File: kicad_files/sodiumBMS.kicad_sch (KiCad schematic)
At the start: 28 parts, among them J1 USB_C_Receptacle_PowerOnly_6P, Q1 AO3400A, U1 STM32F446RETx, U2 INA180A4, U3 INA180A4, U4 LM3940, U5 MC34063AD

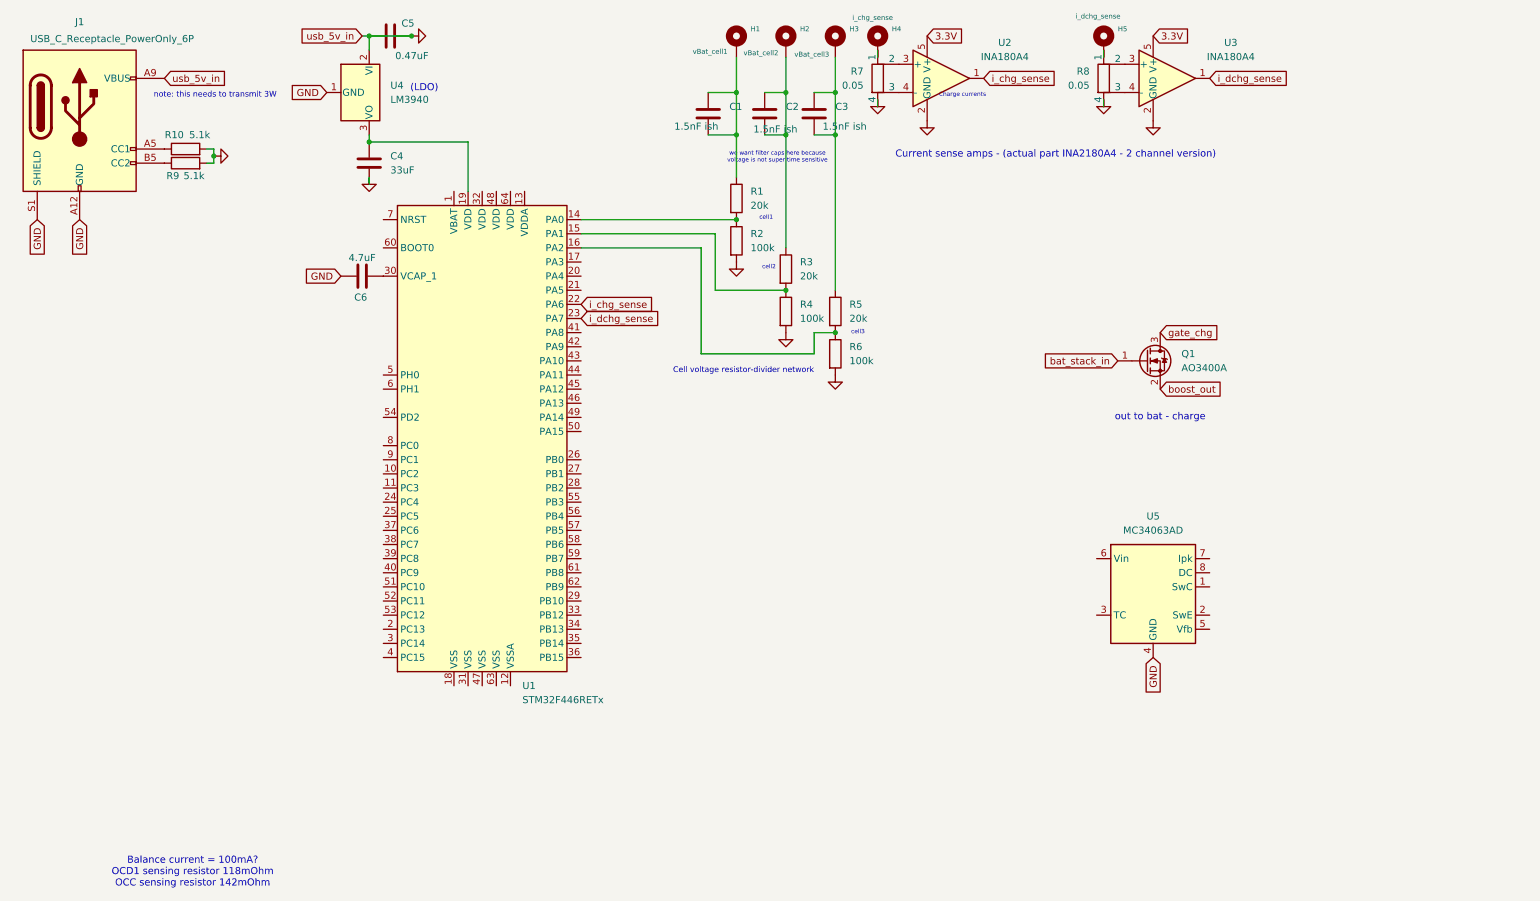
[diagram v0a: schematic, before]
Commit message: added boost converter after deciding on mc34063 with external fet
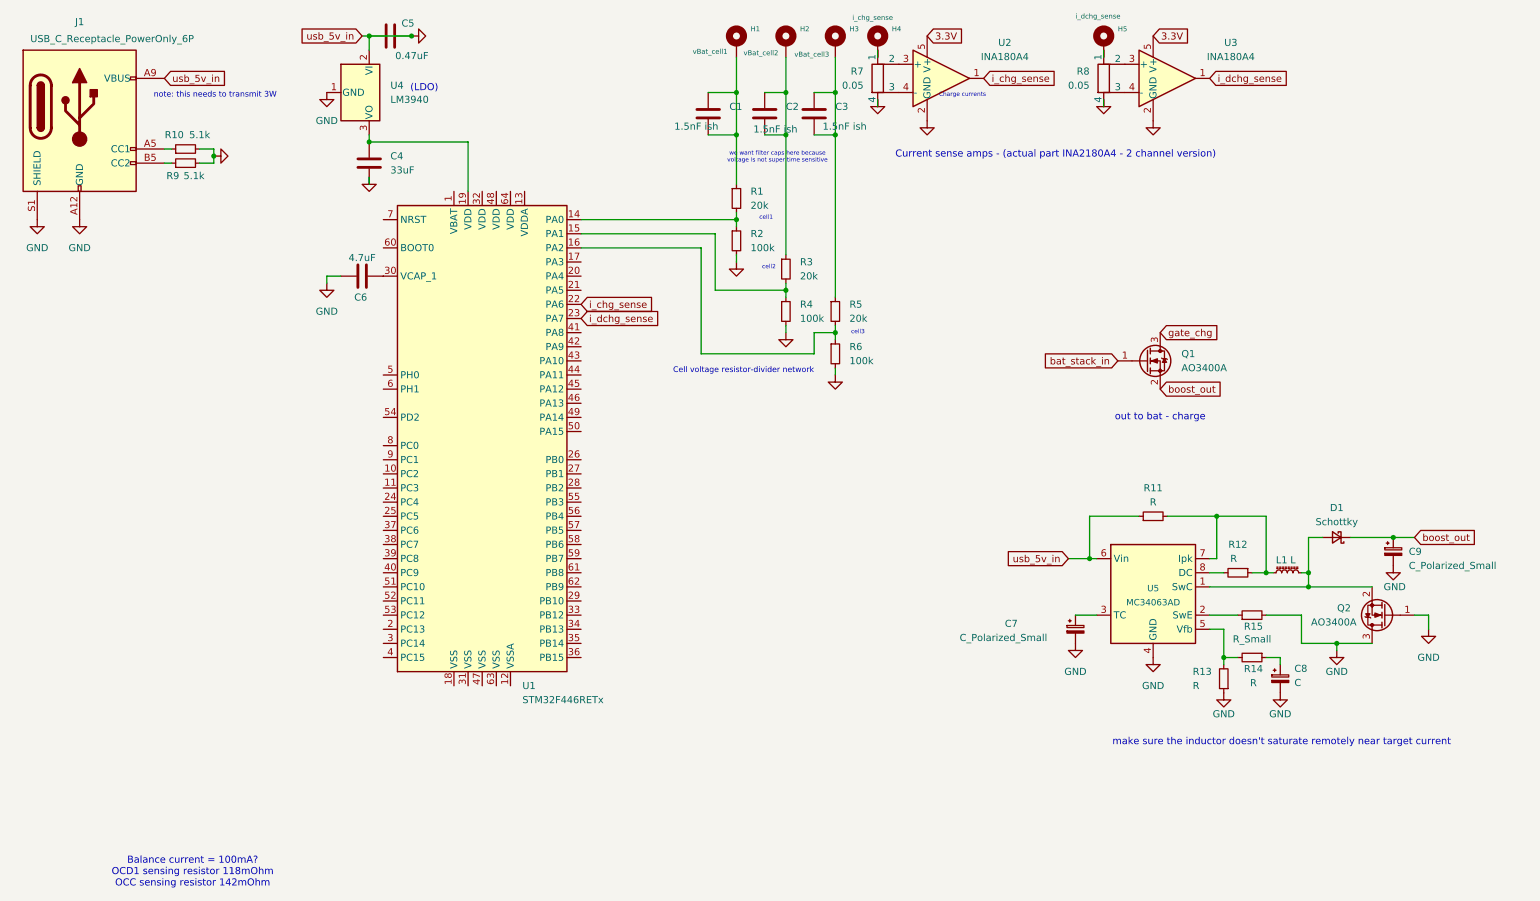
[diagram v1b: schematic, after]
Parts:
- added C7, C9: C_Polarized_Small, symbol Device:C_Polarized_Small
- added C8: C, symbol Device:C_Polarized_Small
- added D1: Schottky, symbol Device:D_Schottky_Small
- added L1: L, symbol Device:L_Ferrite_Small
- added Q2: AO3400A, Package_TO_SOT_SMD:SOT-23, symbol Transistor_FET:AO3400A
- added R11, R12, R13, R14: R, symbol Device:R_Small
- added R15: R_Small, symbol Device:R_Small
- R1, R10, R2, R3, R4, R5, R6, R9: symbol Device:R -> Device:R_Small
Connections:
- net GND: now also U5.6 (Vin), C7.2, C8.2, C9.2, Q2.1 (G), Q2.3 (D), R11.1, R13.1, R15.2
- net boost_out: now also C9.1, D1.1 (K)
- net at U5.1 (SwC): now also D1.2 (A), L1.2, Q2.2 (S)
- net at U5.2 (SwE): now also R15.1
- net at U5.3 (TC): now also C7.1
- net at U5.5 (Vfb): now also R13.2, R14.2
- net at U5.7 (Ipk): now also L1.1, R11.2, R12.1
- net at U5.8 (DC): now also R12.2
- new net: C8.1, R14.1
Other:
- note added: "make sure the inductor doesn't saturate remotely near target current"

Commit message: separate sheets now, pretty much done with schematic just gotta do some documentation
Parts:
- removed C1, C2, C3: 1.5nF ish, symbol Device:C
- removed C7, C9: C_Polarized_Small, symbol Device:C_Polarized_Small
- removed C8: C, symbol Device:C_Polarized_Small
- removed D1: Schottky, symbol Device:D_Schottky_Small
- removed H1: vBat_cell1, symbol Mechanical:MountingHole_Pad
- removed H2: vBat_cell2, symbol Mechanical:MountingHole_Pad
- removed H3: vBat_cell3, symbol Mechanical:MountingHole_Pad
- removed H4: i_chg_sense, symbol Mechanical:MountingHole_Pad
- removed H5: i_dchg_sense, symbol Mechanical:MountingHole_Pad
- removed L1: L, symbol Device:L_Ferrite_Small
- removed Q1, Q2: AO3400A, Package_TO_SOT_SMD:SOT-23, symbol Transistor_FET:AO3400A
- removed R1, R3, R5: 20k, symbol Device:R_Small
- removed R11, R12, R13, R14: R, symbol Device:R_Small
- removed R15: R_Small, symbol Device:R_Small
- removed R2, R4, R6: 100k, symbol Device:R_Small
- removed R7, R8: 0.05, symbol Device:R_Shunt
- removed U2, U3: INA180A4, Package_TO_SOT_SMD:SOT-23-5, symbol Amplifier_Current:INA180A4
- removed U5: MC34063AD, Package_SO:SOIC-8_3.9x4.9mm_P1.27mm, symbol Regulator_Switching:MC34063AD
- added R16: 3.3k, symbol Device:R_Small
- added R17: 30k, symbol Device:R_Small
- added R18: 100k, symbol Device:R_Small
- C4, C5, C6: symbol Device:C -> Device:C_Small
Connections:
- net GND: now also R18.1; no longer C5.1, J1.A9 (VBUS), J1.B9 (VBUS), U4.2 (VI)
- net cell2_vsense: now reaches U1.16 (PA2)
- net cell1_vsense: now reaches U1.15 (PA1)
- net cell3_vsense: now reaches U1.17 (PA3)
- net charge_start: now reaches U1.27 (PB1)
- net out_switch: now reaches U1.28 (PB2)
- net mcu_vdd_3.3v: now reaches U1.32 (VDD)
- net mcu_vdd_3.3v: now also R16.1
- net at U1.43 (PA10): now also R17.1, R18.2
- net at U1.60 (BOOT0): now also R16.2
- new net usb_5v_in: C5.1, J1.A9 (VBUS), J1.B9 (VBUS), R17.2, U4.2 (VI)
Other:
- added sheet Current and Voltage sensing (sensing.kicad_sch)
- added sheet charge power supply (powerSupply.kicad_sch)
- note removed: "Cell voltage resistor-divider network"
- note removed: "Charge currents"
- note removed: "Current sense amps - (actual part INA2180A4 - 2 channel version)"
- note removed: "cell1"
- note removed: "cell2"
- note removed: "cell3"
- note removed: "make sure the inductor doesn't saturate remotely near target current"
- note removed: "out to bat - charge"
- note removed: "we want filter caps here because voltage is not super time sensitive"
- moved on the sheet: C4, C5, C6, J1, R10, R9, U1, U4
